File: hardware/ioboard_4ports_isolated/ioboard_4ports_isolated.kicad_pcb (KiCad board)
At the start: 2 copper layers, 106 x 55 mm, 59 parts, among them J1 Conn_02x06_Odd_Even, J10 XLR3, J11 XLR3, J12 Conn_01x03, J13 Conn_01x03, J14 8P8C, J2 XLR3, J3 XLR3, J4 XLR3, J5 XLR3, J6 Conn_01x03, J7 Conn_01x03, J8 XLR3, J9 XLR3, U1 M24C64-RMN6TP, U2 CRE1S0505DC, U3 CRE1S0505DC, U4 ADM2483xRW, U5 ADM2483xRW, U6 ADM2483xRW, U7 ADM2483xRW

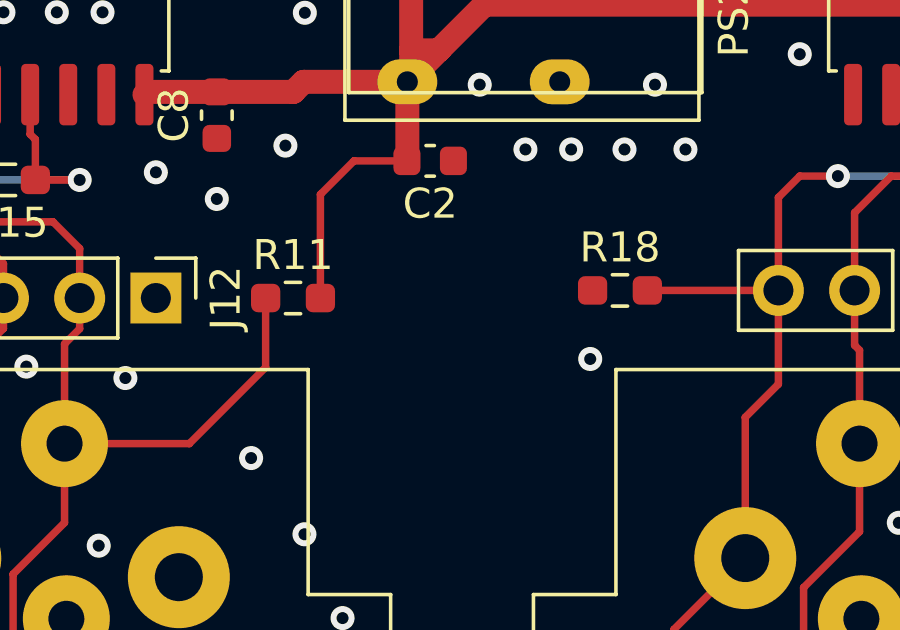
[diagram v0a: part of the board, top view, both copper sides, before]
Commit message: Update ioboards to KiCad 8, add OpenHardware logo
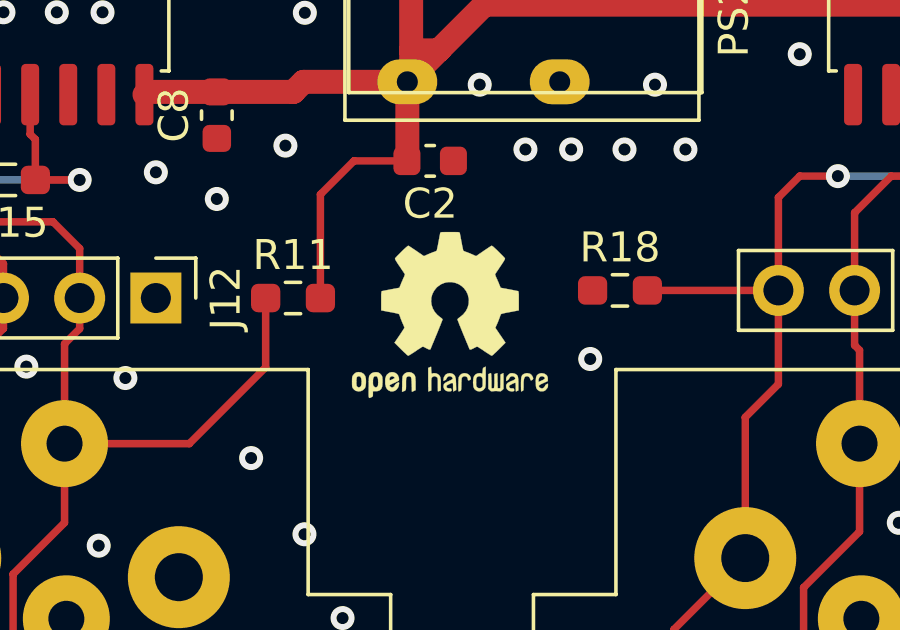
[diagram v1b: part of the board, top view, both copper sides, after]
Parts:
- added SYM1: Logo_Open_Hardware_Small, Symbol:OSHW-Logo2_7.3x6mm_SilkScreen, F.Cu at (104.0, 51.9)
